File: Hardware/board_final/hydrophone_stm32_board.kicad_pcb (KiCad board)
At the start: 4 copper layers, 69.8 x 49.9 mm, 101 parts, among them IC1 AD8031ARZ, J1 Conn_01x02, J2 Conn_02x05_Odd_Even, J3 Conn_01x02, J4 Conn_01x03, J5 47352-1001, J6 142-0701-851, J7 Conn_01x02_Female, U1 AMS1117-3.3, U2 STM32F746ZGT6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

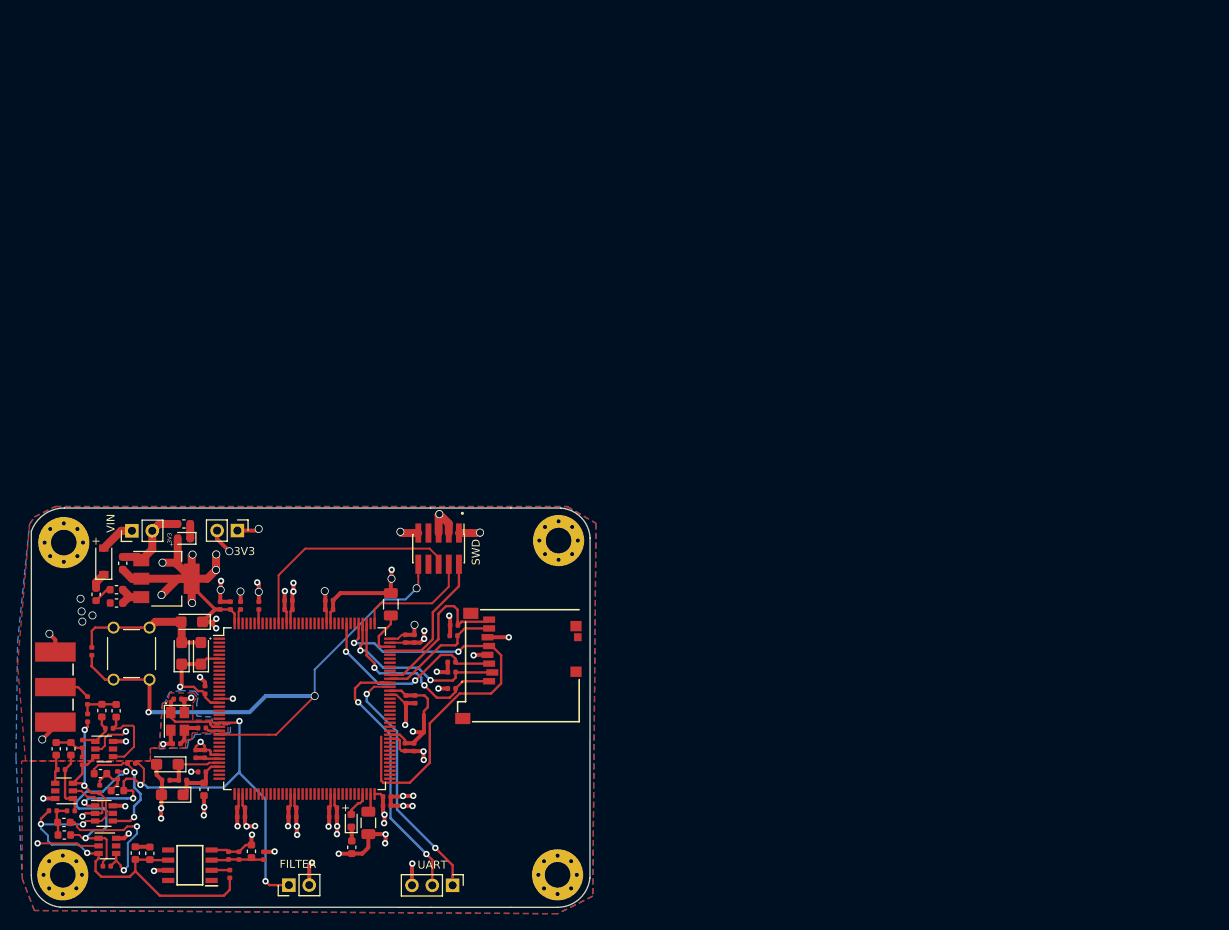
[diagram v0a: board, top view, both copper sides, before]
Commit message: Added F7 100 Pin Version
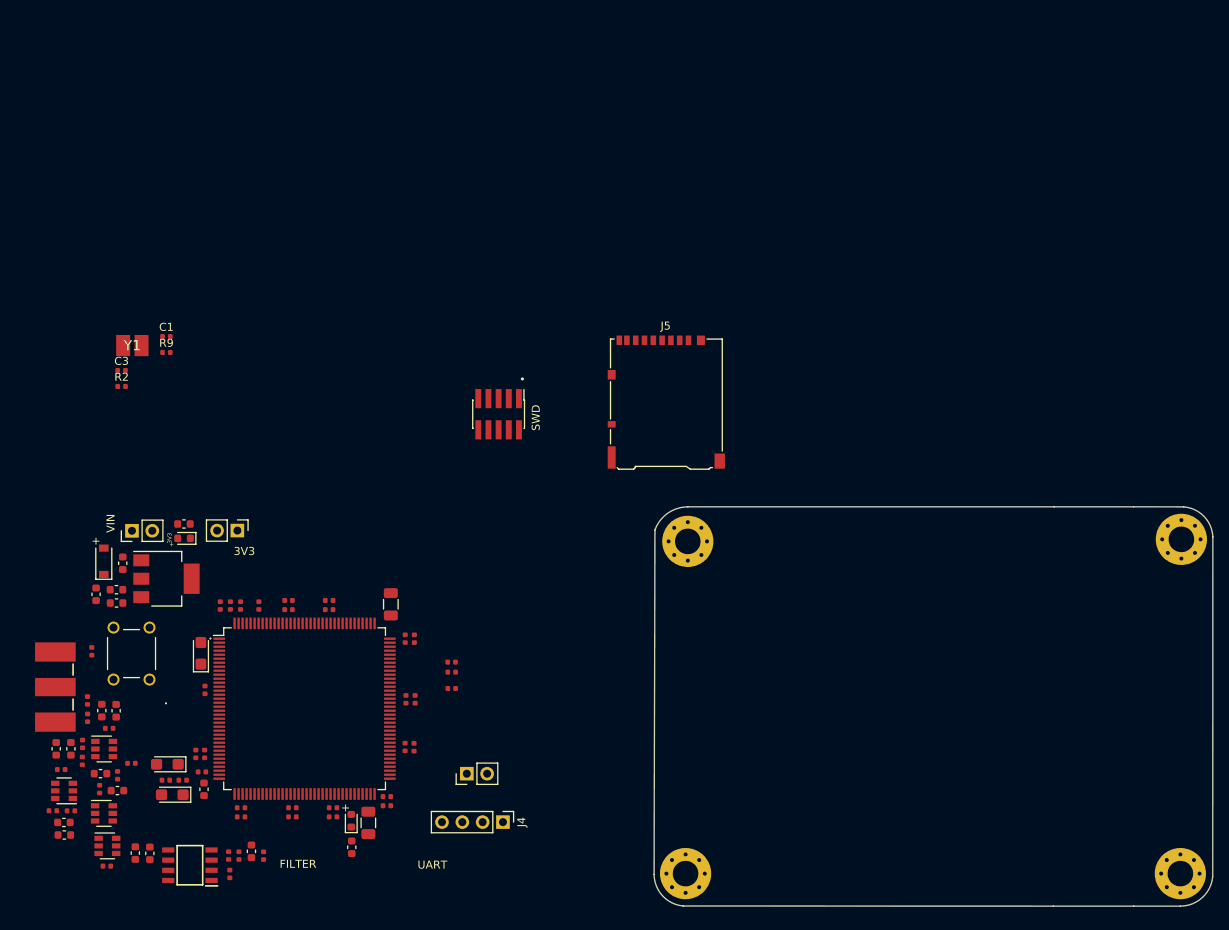
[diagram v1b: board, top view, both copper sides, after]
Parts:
- removed C28, C29: 18p, Capacitor_SMD:C_0402_1005Metric
- removed HSE1: 25MHz, Crystal:Crystal_SMD_3225-4Pin_3.2x2.5mm
- removed R10: 47k, Resistor_SMD:R_0402_1005Metric
- added Y1: Crystal, SamacSys_Parts:RESC3226X100N, F.Cu at (54.5, 26.7)
- C1: value 4.7u -> 4.3p; footprint Capacitor_Tantalum_SMD:CP_EIA-3216-18_Kemet-A -> Capacitor_SMD:C_0402_1005Metric
- C3: value 1u -> 4.3p; footprint Capacitor_Tantalum_SMD:CP_EIA-3216-18_Kemet-A -> Capacitor_SMD:C_0402_1005Metric
- J4: value Conn_01x03 -> Conn_01x04; footprint Connector_PinHeader_2.54mm:PinHeader_1x03_P2.54mm_Vertical -> Connector_PinHeader_2.54mm:PinHeader_1x04_P2.54mm_Vertical
- J5: value 47352-1001 -> Micro_SD_Card; footprint SamacSys_Parts:47352-1001 -> Connector_Card:microSD_HC_Hirose_DM3AT-SF-PEJM5
- R2: value 100 -> 47k
- moved H2 78.0 mm to (124.0, 51.2)
- moved H1 77.9 mm to (185.7, 50.9)
- moved H3 77.9 mm to (123.7, 92.7)
- moved H4 77.9 mm to (185.5, 92.7)
- moved R9 49.6 mm to (58.8, 27.5), turned to 0 degrees
- moved J5 47.7 mm to (121.3, 33.8), turned to 0 degrees
- moved R2 43.9 mm to (53.2, 31.8), turned to 0 degrees
- moved C1 39.6 mm to (58.8, 25.6), turned to 0 degrees
- moved C3 32.6 mm to (53.2, 29.8), turned to 0 degrees
- moved J7 26.2 mm to (96.3, 80.2)
- moved J2 18.4 mm to (100.3, 35.3)
- moved J4 10.1 mm to (100.9, 86.2)
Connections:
- net VREF renamed VDIV
- C1 pad 1: 3V3 -> Net-(C1-Pad1)
- C10 pad 1: 3V3 -> +3V3
- C11 pad 1: 3V3 -> +3V3
- C12 pad 1: 3V3 -> +3V3
- C13 pad 1: 3V3 -> +3V3
- C14 pad 1: 3V3 -> +3V3
- C15 pad 1: 3V3 -> +3V3
- C16 pad 1: 3V3 -> +3V3
- C17 pad 1: 3V3 -> +3V3
- C18 pad 1: 3V3 -> +3V3
- C19 pad 1: 3V3 -> +3V3
- C2 pad 1: 3V3 -> +3V3
- C20 pad 1: 3V3 -> +3V3
- C21 pad 1: 3V3 -> +3V3
- C22 pad 1: 3V3 -> +3V3
- C23 pad 1: 3V3 -> +3V3
- C24 pad 1: 3V3 -> +3V3
- C25 pad 1: 3V3 -> +3V3
- C26 pad 1: 3V3 -> +3V3
- C3 pad 1: 3V3 -> Net-(C3-Pad1)
- C32 pad 1: 3V3 -> +3V3
- C4 pad 1: 3V3 -> +3V3
- C5 pad 1: 3V3 -> +3V3
- C6 pad 1: 3V3 -> +3V3
- C7 pad 1: 3V3 -> +3V3
- C8 pad 1: 3V3 -> +3V3
- C9 pad 1: 3V3 -> +3V3
- D1 pad 2: 3V3 -> +3V3
- FB2 pad 2: 3V3 -> +3V3
- IC1 pad 7: 3V3 -> Net-(IC1-Pad7)
- J2 pad 1: 3V3 -> +3V3
- J3 pad 1: 3V3 -> +3V3
- J4 pad 3: GND -> +3V3
- J5 pad 4: 3V3 -> +3V3
- J5 pad 9: (no net) -> GND
- R14 pad 2: 3V3 -> +3V3
- R2 pad 1: HSE_OUT -> uSD_D0
- R2 pad 2: Net-(C29-Pad1) -> +3V3
- R5 pad 1: 3V3 -> PDR_ON
- R5 pad 2: PDR_ON -> +3V3
- R6 pad 2: 3V3 -> +3V3
- R7 pad 2: 3V3 -> +3V3
- R8 pad 2: 3V3 -> +3V3
- R9 pad 2: 3V3 -> +3V3
- U1 pad 2: 3V3 -> +3V3
- U2 pad 108: 3V3 -> +3V3
- U2 pad 121: 3V3 -> +3V3
- U2 pad 131: 3V3 -> +3V3
- U2 pad 144: 3V3 -> +3V3
- U2 pad 17: 3V3 -> +3V3
- U2 pad 23: HSE_IN -> Net-(C1-Pad1)
- U2 pad 24: HSE_OUT -> Net-(C3-Pad1)
- U2 pad 30: 3V3 -> +3V3
- U2 pad 39: 3V3 -> +3V3
- U2 pad 52: 3V3 -> +3V3
- U2 pad 6: 3V3 -> +3V3
- U2 pad 62: 3V3 -> +3V3
- U2 pad 72: 3V3 -> +3V3
- U2 pad 84: 3V3 -> +3V3
- U2 pad 95: 3V3 -> +3V3
- U3 pad 6: 3V3 -> +3V3
- U4 pad 6: 3V3 -> +3V3
- U5 pad 6: 3V3 -> +3V3
- U6 pad 6: 3V3 -> +3V3
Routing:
- net GND: track 183.0 -> 0.00 mm, vias 46 -> 0
- net 3V3: track 145.7 -> 0.00 mm, vias 37 -> 0
- net NRST: track 72.3 -> 0.00 mm, vias 3 -> 0
- net VDIV: track 68.8 -> 0.00 mm, vias 5 -> 0
- net V_OUT: track 57.5 -> 0.00 mm, vias 5 -> 0
- net uSD_CLK: track 54.4 -> 0.00 mm, vias 2 -> 0
- net USART6_RX: track 33.6 -> 0.00 mm, vias 2 -> 0
- net USART6_TX: track 31.6 -> 0.00 mm, vias 2 -> 0
- net SWO: track 28.7 -> 0.00 mm
- net Net-(C44-Pad1): track 26.8 -> 0.00 mm, vias 2 -> 0
- net uSD_CMD: track 26.1 -> 0.00 mm, vias 2 -> 0
- net uSD_D2: track 23.3 -> 0.00 mm, vias 2 -> 0
- net uSD_D3: track 22.5 -> 0.00 mm, vias 2 -> 0
- net uSD_D1: track 20.9 -> 0.00 mm
- net Net-(C48-Pad1): track 18.7 -> 0.00 mm, vias 2 -> 0
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- removed copper zone on 3V3, net 3V3
- removed copper zone on B.Cu, net GND
- removed copper zone on F.Cu, net GND
- removed copper zone on GND, net GND
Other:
- outline, holes or cut-outs redrawn

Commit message: Added 100 pin version
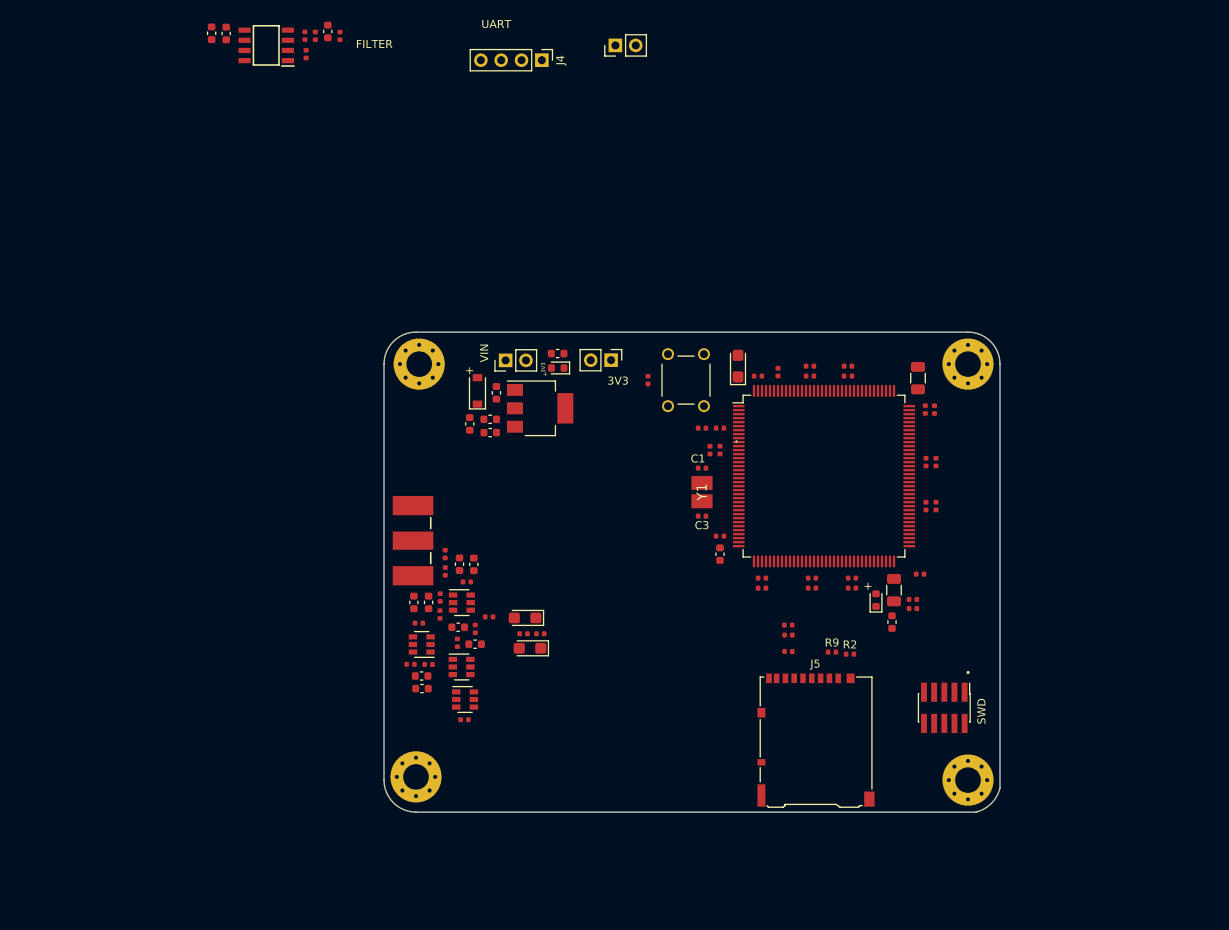
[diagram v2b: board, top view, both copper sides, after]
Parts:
- moved C38 102.9 mm to (66.3, -12.3)
- moved C39 102.9 mm to (64.5, -12.4)
- moved IC1 102.9 mm to (71.3, -10.8)
- moved R16 102.9 mm to (76.3, -9.75)
- moved C40 102.9 mm to (79.0, -12.6)
- moved C41 102.9 mm to (77.4, -12.0)
- moved R14 102.9 mm to (80.5, -12.0)
- moved R15 102.9 mm to (76.1, -12.0)
- moved R2 97.0 mm to (144.2, 65.2)
- moved J4 95.4 mm to (105.7, -8.99)
- moved J7 92.9 mm to (114.9, -10.8)
- moved R9 91.2 mm to (142.0, 65.0)
- moved C11 79.4 mm to (153.0, 55.2)
- moved C7 77.4 mm to (139.5, 55.8)
- moved C27 77.3 mm to (119.0, 31.0)
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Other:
- board size 69.8 x 49.9 mm -> 77 x 60 mm
